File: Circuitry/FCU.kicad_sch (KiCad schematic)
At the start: 29 parts, among them J1 Conn_01x04_Pin, J2 USB_C_Receptacle_USB2.0_16P, J3 Conn_01x06_Pin, J4 Conn_01x04_Pin, J5 Conn_01x04_Pin, SW1 SW_SPDT, SW2 SW_Push, U1 STM32F405RGTx, U2 AMS1117-3.3, Y1 8MHz

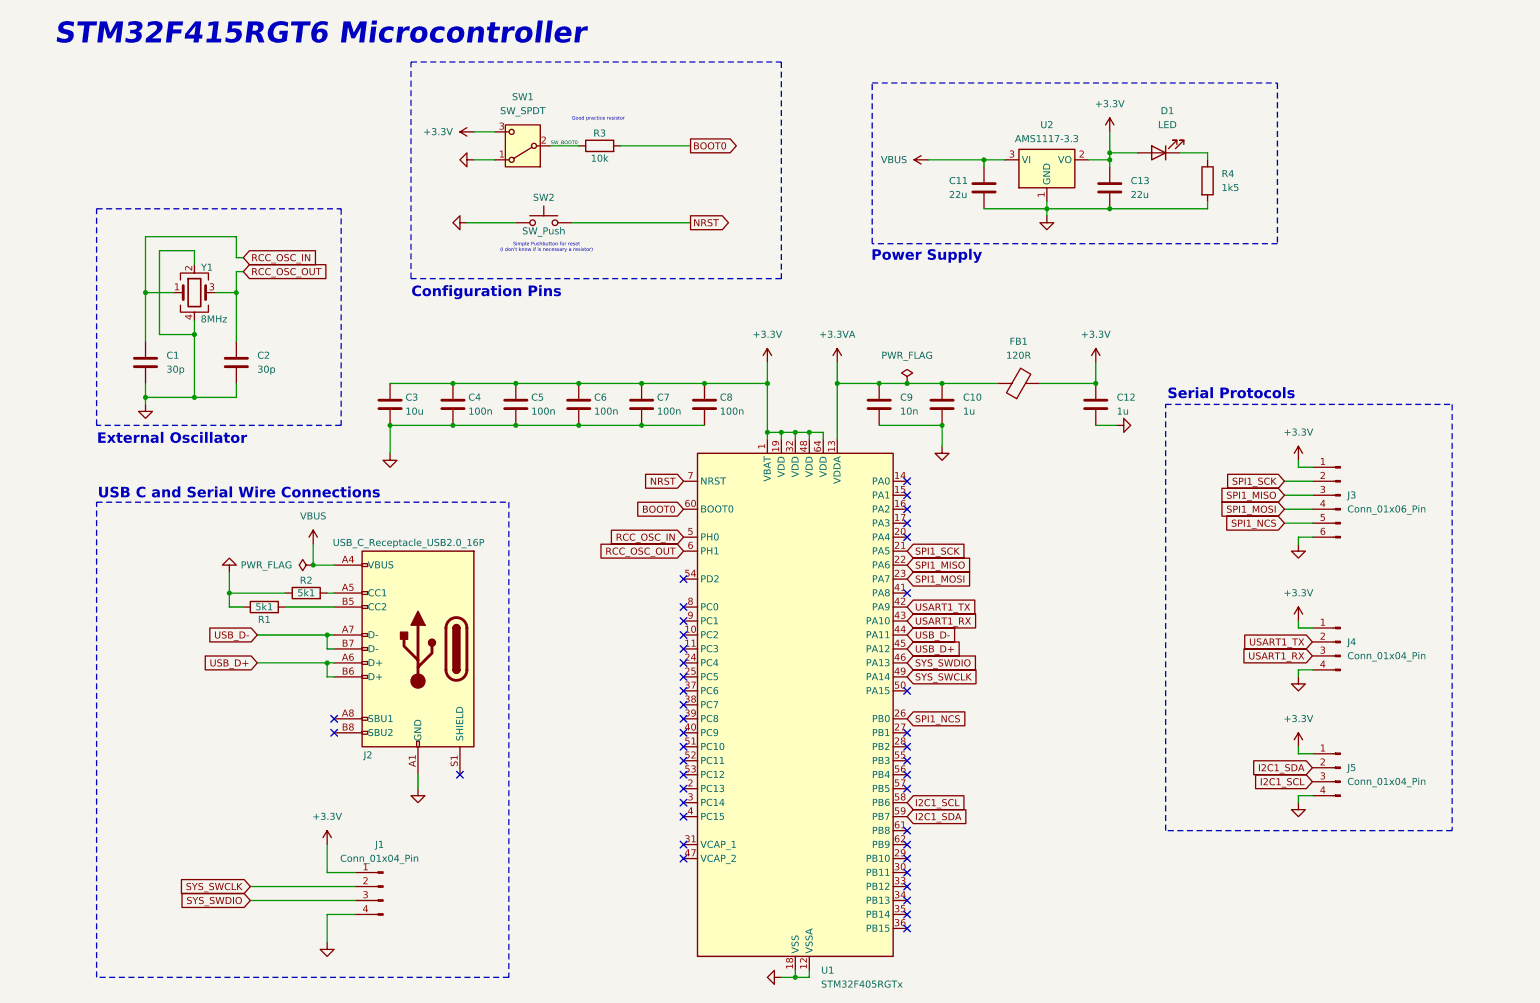
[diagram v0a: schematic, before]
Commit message: created FCU symbol and footprint libraries, add documentation, did some tests in STM32 project
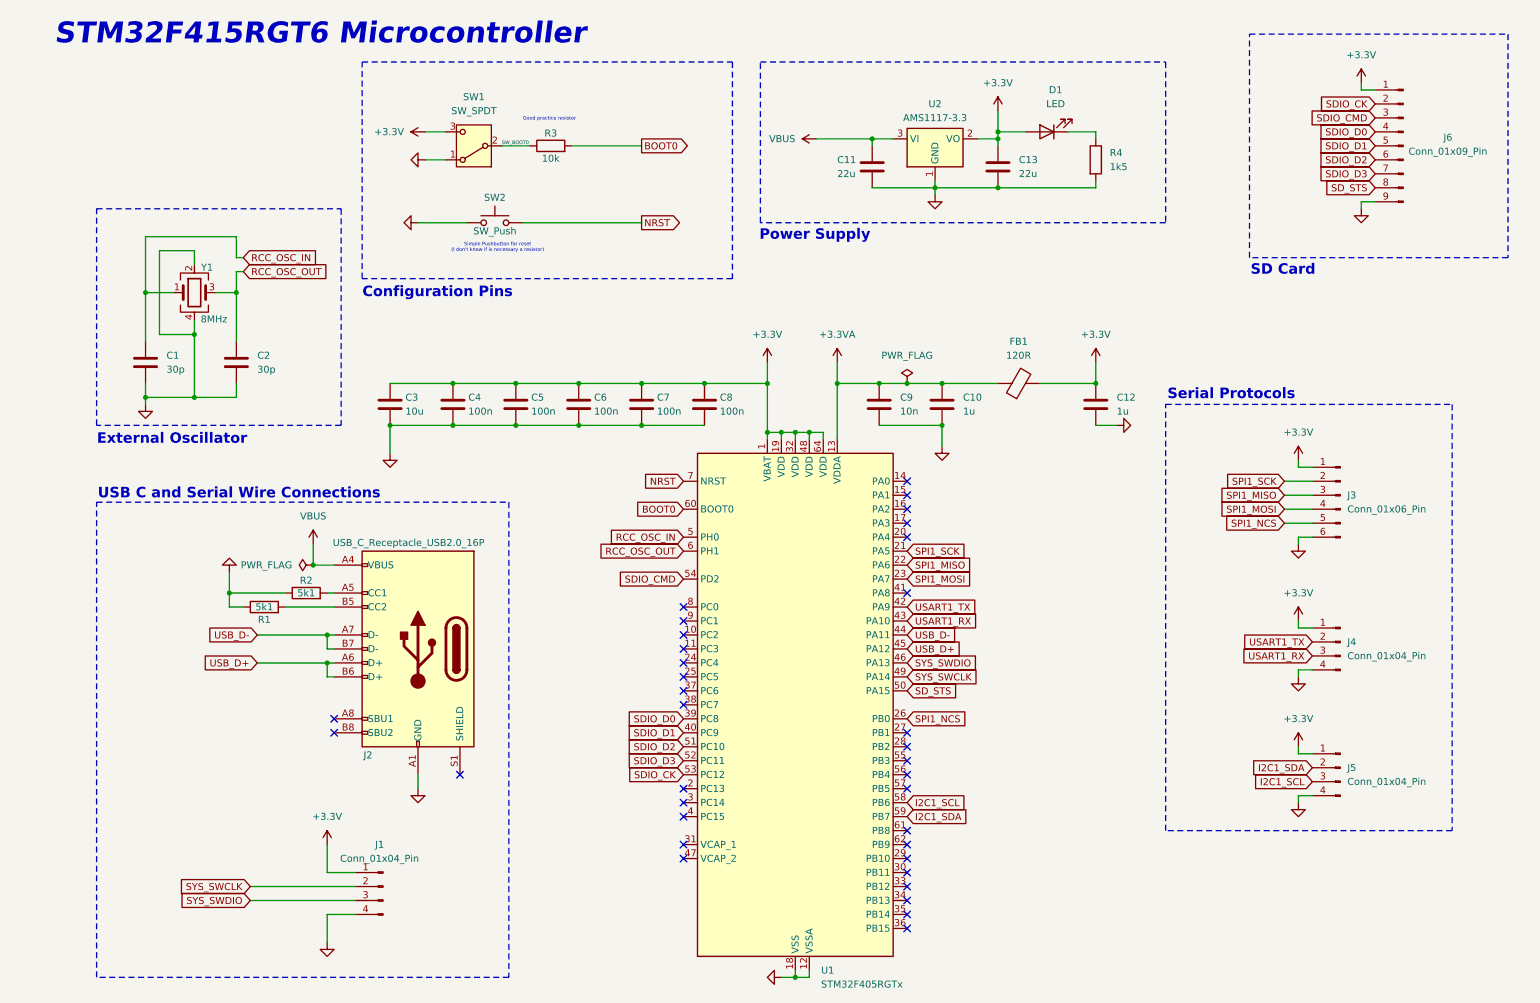
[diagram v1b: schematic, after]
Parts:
- added J6: Conn_01x09_Pin, Connector_JST:JST_PH_S9B-PH-K_1x09_P2.00mm_Horizontal, symbol Connector:Conn_01x09_Pin
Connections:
- net +3.3V: now also J6.1 (Pin_1)
- net GND: now also J6.9 (Pin_9)
- net SDIO_D0: now reaches U1.39 (PC8)
- net SDIO_D0: now also J6.4 (Pin_4)
- net SDIO_D1: now reaches U1.40 (PC9)
- net SDIO_D1: now also J6.5 (Pin_5)
- net SD_STS: now reaches U1.50 (PA15)
- net SD_STS: now also J6.8 (Pin_8)
- net SDIO_D2: now reaches U1.51 (PC10)
- net SDIO_D2: now also J6.6 (Pin_6)
- net SDIO_D3: now reaches U1.52 (PC11)
- net SDIO_D3: now also J6.7 (Pin_7)
- net SDIO_CK: now reaches U1.53 (PC12)
- net SDIO_CK: now also J6.2 (Pin_2)
- net SDIO_CMD: now reaches U1.54 (PD2)
- net SDIO_CMD: now also J6.3 (Pin_3)
- no-connect marks 42 -> 35
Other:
- note added: "SD Card"
- moved on the sheet: C11, C13, D1, R3, R4, SW1, SW2, U2

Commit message: added some readme notes
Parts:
- removed J6: Conn_01x09_Pin, Connector_JST:JST_PH_S9B-PH-K_1x09_P2.00mm_Horizontal, symbol Connector:Conn_01x09_Pin
- added C14: 10uF, Capacitor_SMD:C_1206_3216Metric, symbol Device:C
- added C15: 100n, Capacitor_SMD:C_0603_1608Metric, symbol Device:C
- added J6: SD_Card_Receptacle, Connector_Card:SD_Hirose_DM1AA_SF_PEJ82, symbol Connector:SD_Card_Receptacle
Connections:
- net +3.3V: now also C14.1, C15.1, J6.4 (VDD)
- net GND: now also C14.2, C15.2, J6.12 (SHELL1), J6.13 (SHELL2), J6.3 (VSS), J6.6 (VSS)
- net SDIO_CK: now also J6.5 (CLK)
- net SDIO_CMD: now also J6.2 (CMD)
- net SDIO_D0: now also J6.7 (DAT0)
- net SDIO_D1: now also J6.8 (DAT1)
- net SDIO_D2: now also J6.9 (DAT2)
- net SDIO_D3: now also J6.1 (CD/DAT3)
- net SD_STS: now also J6.10 (CARD_DETECT)
